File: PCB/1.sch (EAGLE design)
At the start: 52 parts, among them IC1 7805, IC2 MEGA32-P, T1 2N2219, T2 2N2219, T3 2N2219, T4 2N2219, T5 BC337, T6 BC337, T7 BC337, X1 9v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

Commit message: Fix PCB
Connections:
- net N$44: now also X2-1.KL; no longer X2-2.KL
- net SW1: now also X6-1.KL; no longer X6-2.KL
- net VCC: now also X2-2.KL, X6-2.KL; no longer X2-1.KL, X6-1.KL
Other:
- moved on the sheet: X2-1, X2-2, X6-1, X6-2
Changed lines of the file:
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@@
 <instance part="GND1" gate="1" x="60.96" y="35.56"/>
 <instance part="P+1" gate="VCC" x="93.98" y="59.69"/>
-<instance part="X2" gate="-1" x="93.98" y="49.53" rot="R90"/>
-<instance part="X2" gate="-2" x="78.74" y="59.69" rot="R180"/>
+<instance part="X2" gate="-1" x="78.74" y="59.69" rot="R180"/>
+<instance part="X2" gate="-2" x="93.98" y="49.53" rot="R90"/>
 </instances>
 <busses>
@@
 <pinref part="R1" gate="G$1" pin="2"/>
 <wire x1="73.66" y1="53.34" x2="71.12" y2="53.34" width="0.1524" layer="91"/>
-<pinref part="X2" gate="-2" pin="KL"/>
+<pinref part="X2" gate="-1" pin="KL"/>
 <wire x1="73.66" y1="59.69" x2="71.12" y2="59.69" width="0.1524" layer="91"/>
 <junction x="71.12" y="59.69"/>
@@
 <net name="VCC" class="0">
 <segment>
+<pinref part="X2" gate="-2" pin="KL"/>
 <pinref part="P+1" gate="VCC" pin="VCC"/>
-<pinref part="X2" gate="-1" pin="KL"/>
-<wire x1="93.98" y1="57.15" x2="93.98" y2="54.61" width="0.1524" layer="91"/>
+<wire x1="93.98" y1="54.61" x2="93.98" y2="57.15" width="0.1524" layer="91"/>
 </segment>
 </net>
@@
 <instance part="GND10" gate="1" x="204.47" y="12.7"/>
 <instance part="GND11" gate="1" x="212.09" y="12.7"/>
-<instance part="X6" gate="-1" x="194.31" y="24.13" rot="R180"/>
-<instance part="X6" gate="-2" x="196.85" y="29.21"/>
+<instance part="X6" gate="-1" x="196.85" y="29.21"/>
+<instance part="X6" gate="-2" x="194.31" y="24.13" rot="R180"/>
 <instance part="X7" gate="-1" x="219.71" y="29.21" rot="R180"/>
 <instance part="X7" gate="-2" x="224.79" y="24.13"/>
@@
 <pinref part="P+5" gate="VCC" pin="VCC"/>
 <wire x1="187.96" y1="26.67" x2="187.96" y2="24.13" width="0.1524" layer="91"/>
-<pinref part="X6" gate="-1" pin="KL"/>
-<wire x1="187.96" y1="24.13" x2="189.23" y2="24.13" width="0.1524" layer="91"/>
+<pinref part="X6" gate="-2" pin="KL"/>
+<wire x1="189.23" y1="24.13" x2="187.96" y2="24.13" width="0.1524" layer="91"/>
 </segment>
 </net>
@@
 <label x="203.2" y="31.75" size="1.778" layer="95"/>
 <wire x1="204.47" y1="27.94" x2="204.47" y2="29.21" width="0.1524" layer="91"/>
-<pinref part="X6" gate="-2" pin="KL"/>
+<pinref part="X6" gate="-1" pin="KL"/>
 <wire x1="204.47" y1="29.21" x2="204.47" y2="31.75" width="0.1524" layer="91"/>
 <wire x1="201.93" y1="29.21" x2="204.47" y2="29.21" width="0.1524" layer="91"/>

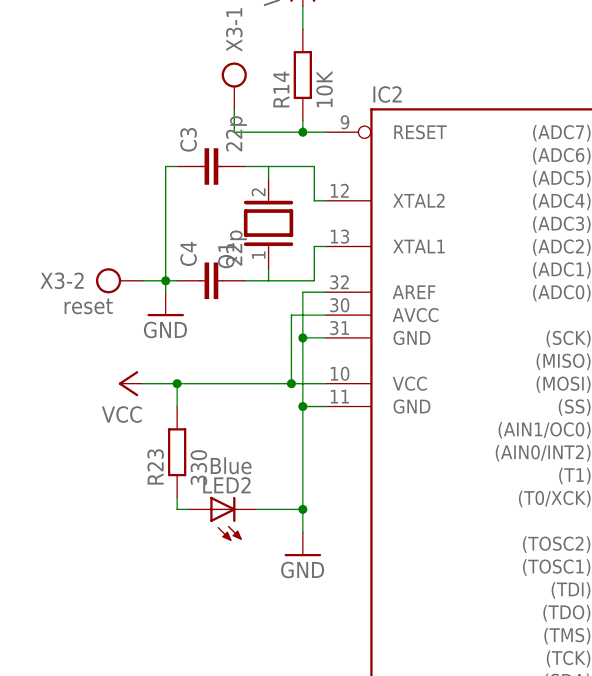
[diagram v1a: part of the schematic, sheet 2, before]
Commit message: Fix PCB (PCB is working)
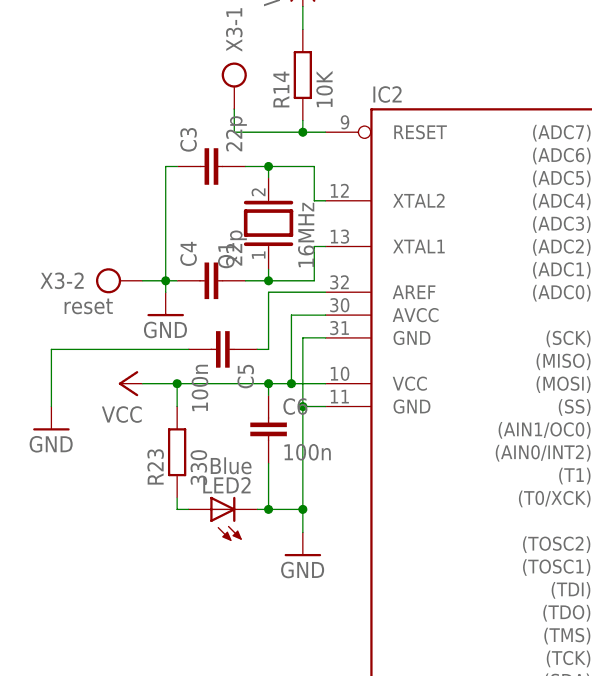
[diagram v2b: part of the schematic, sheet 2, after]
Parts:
- added C5, C6: 100n, rcl:C-EU025-024X044
- Q1: value (none) -> 16MHz
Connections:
- new net N$45: C5.1, IC2.AREF
- net GND: now also C5.2, C6.2; no longer IC2.AREF
- net N$44: now also X2-2.KL; no longer X2-1.KL
- net VCC: now also C6.1, X2-1.KL; no longer X2-2.KL
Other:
- moved on the sheet: X2-1, X2-2
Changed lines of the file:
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@@
 <part name="P+2" library="supply1" deviceset="VCC" device=""/>
 <part name="GND3" library="supply1" deviceset="GND" device=""/>
-<part name="Q1" library="special" deviceset="XTAL" device=""/>
+<part name="Q1" library="special" deviceset="XTAL" device="" value="16MHz"/>
 <part name="C3" library="rcl" deviceset="C-EU" device="025-024X044" value="22p"/>
 <part name="C4" library="rcl" deviceset="C-EU" device="025-024X044" value="22p"/>
@@
 <part name="P+6" library="supply1" deviceset="VCC" device=""/>
 <part name="R23" library="rcl" deviceset="R-EU_" device="0204/7" value="330"/>
+<part name="C5" library="rcl" deviceset="C-EU" device="025-024X044" value="100n"/>
+<part name="GND12" library="supply1" deviceset="GND" device=""/>
+<part name="C6" library="rcl" deviceset="C-EU" device="025-024X044" value="100n"/>
 </parts>
 <sheets>
@@
 <instance part="GND1" gate="1" x="60.96" y="35.56"/>
 <instance part="P+1" gate="VCC" x="93.98" y="59.69"/>
-<instance part="X2" gate="-1" x="78.74" y="59.69" rot="R180"/>
-<instance part="X2" gate="-2" x="93.98" y="49.53" rot="R90"/>
+<instance part="X2" gate="-1" x="93.98" y="49.53" rot="R90"/>
+<instance part="X2" gate="-2" x="78.74" y="59.69" rot="R180"/>
 </instances>
 <busses>
@@
 <pinref part="R1" gate="G$1" pin="2"/>
 <wire x1="73.66" y1="53.34" x2="71.12" y2="53.34" width="0.1524" layer="91"/>
-<pinref part="X2" gate="-1" pin="KL"/>
+<pinref part="X2" gate="-2" pin="KL"/>
 <wire x1="73.66" y1="59.69" x2="71.12" y2="59.69" width="0.1524" layer="91"/>
 <junction x="71.12" y="59.69"/>
@@
 <net name="VCC" class="0">
 <segment>
-<pinref part="X2" gate="-2" pin="KL"/>
+<pinref part="X2" gate="-1" pin="KL"/>
 <pinref part="P+1" gate="VCC" pin="VCC"/>
 <wire x1="93.98" y1="54.61" x2="93.98" y2="57.15" width="0.1524" layer="91"/>
@@
 <instance part="P+6" gate="VCC" x="231.14" y="29.21"/>
 <instance part="R23" gate="G$1" x="106.68" y="78.74" rot="R90"/>
+<instance part="C5" gate="G$1" x="113.03" y="90.17" rot="R270"/>
+<instance part="GND12" gate="1" x="92.71" y="81.28"/>
+<instance part="C6" gate="G$1" x="116.84" y="82.55"/>
 </instances>
 <busses>
@@
 <wire x1="123.19" y1="91.44" x2="120.65" y2="91.44" width="0.1524" layer="91"/>
 <wire x1="120.65" y1="91.44" x2="120.65" y2="83.82" width="0.1524" layer="91"/>
-<pinref part="IC2" gate="G$1" pin="AREF"/>
-<wire x1="123.19" y1="96.52" x2="120.65" y2="96.52" width="0.1524" layer="91"/>
-<wire x1="120.65" y1="96.52" x2="120.65" y2="91.44" width="0.1524" layer="91"/>
-<junction x="120.65" y="91.44"/>
 <junction x="120.65" y="83.82"/>
 <pinref part="LED2" gate="G$1" pin="C"/>
-<wire x1="115.57" y1="72.39" x2="120.65" y2="72.39" width="0.1524" layer="91"/>
+<wire x1="115.57" y1="72.39" x2="116.84" y2="72.39" width="0.1524" layer="91"/>
 <junction x="120.65" y="72.39"/>
+<pinref part="C6" gate="G$1" pin="2"/>
+<wire x1="116.84" y1="72.39" x2="120.65" y2="72.39" width="0.1524" layer="91"/>
+<wire x1="116.84" y1="77.47" x2="116.84" y2="72.39" width="0.1524" layer="91"/>
+<junction x="116.84" y="72.39"/>
 </segment>
 <segment>
@@
 <wire x1="212.09" y1="17.78" x2="212.09" y2="15.24" width="0.1524" layer="91"/>
 </segment>
+<segment>
+<pinref part="C5" gate="G$1" pin="2"/>
+<wire x1="107.95" y1="90.17" x2="92.71" y2="90.17" width="0.1524" layer="91"/>
+<wire x1="92.71" y1="90.17" x2="92.71" y2="83.82" width="0.1524" layer="91"/>
+<pinref part="GND12" gate="1" pin="GND"/>
+</segment>
 </net>
 <net name="N$21" class="0">
@@
 <wire x1="123.19" y1="86.36" x2="119.38" y2="86.36" width="0.1524" layer="91"/>
 <pinref part="IC2" gate="G$1" pin="AVCC"/>
-<wire x1="119.38" y1="86.36" x2="106.68" y2="86.36" width="0.1524" layer="91"/>
+<wire x1="119.38" y1="86.36" x2="116.84" y2="86.36" width="0.1524" layer="91"/>
+<wire x1="116.84" y1="86.36" x2="106.68" y2="86.36" width="0.1524" layer="91"/>
 <wire x1="106.68" y1="86.36" x2="102.87" y2="86.36" width="0.1524" layer="91"/>
 <wire x1="123.19" y1="93.98" x2="119.38" y2="93.98" width="0.1524" layer="91"/>
@@
 <wire x1="106.68" y1="83.82" x2="106.68" y2="86.36" width="0.1524" layer="91"/>
 <junction x="106.68" y="86.36"/>
+<pinref part="C6" gate="G$1" pin="1"/>
+<wire x1="116.84" y1="85.09" x2="116.84" y2="86.36" width="0.1524" layer="91"/>
+<junction x="116.84" y="86.36"/>
 </segment>
 <segment>
@@
 <pinref part="C3" gate="G$1" pin="2"/>
 <wire x1="114.3" y1="110.49" x2="116.84" y2="110.49" width="0.1524" layer="91"/>
+<junction x="116.84" y="110.49"/>
 </segment>
 </net>
@@
 <pinref part="C4" gate="G$1" pin="2"/>
 <wire x1="116.84" y1="97.79" x2="114.3" y2="97.79" width="0.1524" layer="91"/>
+<junction x="116.84" y="97.79"/>
 </segment>
 </net>
@@
 </segment>
 </net>
+<net name="N$45" class="0">
+<segment>
+<pinref part="IC2" gate="G$1" pin="AREF"/>
+<wire x1="123.19" y1="96.52" x2="116.84" y2="96.52" width="0.1524" layer="91"/>
+<wire x1="116.84" y1="96.52" x2="116.84" y2="90.17" width="0.1524" layer="91"/>
+<pinref part="C5" gate="G$1" pin="1"/>
+<wire x1="116.84" y1="90.17" x2="115.57" y2="90.17" width="0.1524" layer="91"/>
+</segment>
+</net>
 </nets>
 </sheet>
 </sheets>
+<errors>
+</errors>
 </schematic>
 </drawing>

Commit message: Edit timer and PCB
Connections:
- net INT2: now also IC2.(AIN0/INT2)PB2; no longer IC2.(T1)PB1
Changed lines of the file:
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@@
 <net name="INT2" class="0">
 <segment>
-<pinref part="IC2" gate="G$1" pin="(T1)PB1"/>
-<wire x1="163.83" y1="76.2" x2="167.64" y2="76.2" width="0.1524" layer="91"/>
 <wire x1="167.64" y1="76.2" x2="167.64" y2="74.93" width="0.1524" layer="91"/>
 <pinref part="R20" gate="G$1" pin="1"/>
@@
 <wire x1="167.64" y1="76.2" x2="181.61" y2="76.2" width="0.1524" layer="91"/>
 <label x="181.61" y="77.47" size="1.778" layer="95"/>
+<pinref part="IC2" gate="G$1" pin="(AIN0/INT2)PB2"/>
+<wire x1="163.83" y1="78.74" x2="167.64" y2="78.74" width="0.1524" layer="91"/>
+<wire x1="167.64" y1="78.74" x2="167.64" y2="76.2" width="0.1524" layer="91"/>
 <junction x="167.64" y="76.2"/>
 </segment>
